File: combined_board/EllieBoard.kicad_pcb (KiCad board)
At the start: 2 copper layers, 54 parts, among them J1 Load Cell 1.1, J13 Load Cell 4.1, J14 Load Cell 5.1, J15 Load Cell 6.1, J2 Servo Conn 1, J22 Load Cell 7.1, J23 Load Cell 8.1, J28 Flow Meter Conn 2, J29 Servo Conn 2, J3 Servo Conn 3, J30 Servo Conn 4, J32 Load Cell 1.2, J33 Load Cell 2.2, J34 Load Cell 3.2, J35 Load Cell 4.2, J36 Load Cell 5.2, J37 Load Cell 6.2, J38 Load Cell 7.2, J39 Load Cell 8.2, J4 NC Conn, J41 Flow Meter Conn 1, J43 NC Conn, J5 NC Conn 2, J6 Load Cell 2.1, J7 NC Conn 2, J8 Load Cell 3.1, U1 HX711_Breakout, U10 HX711_Breakout, U11 HX711_Breakout, U2 HX711_Breakout, U3 Relay_Board, U4 SD_Card_Reader, U5 HX711_Breakout, U6 HX711_Breakout, U7 ESP32-DEVKITC-32D, U8 HX711_Breakout, U9 HX711_Breakout

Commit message: some updates to layout, not 100% done yet
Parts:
- moved R2 29.3 mm to (24.8, 144.8)
- moved U5 29.2 mm to (141.0, 99.1)
- moved J15 28.6 mm to (141.7, 154.4)
- moved J2 28.6 mm to (135.3, 34.3)
- moved J22 28.6 mm to (163.3, 154.3)
- moved J29 28.6 mm to (135.3, 19.1)
- moved J30 28.6 mm to (116.3, 19.1)
- moved J37 28.6 mm to (141.6, 165.1)
- moved J39 28.6 mm to (186.0, 165.1)
- moved J43 28.6 mm to (167.0, 33.0)
- moved J5 28.6 mm to (166.8, 21.1)
- moved R12 28.6 mm to (186.3, 146.1)
- moved R14 28.6 mm to (139.0, 146.0)
- moved R6 28.6 mm to (157.6, 145.9)
- moved U2 28.6 mm to (141.6, 127.0)
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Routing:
- net GND: track 0.00 -> 978.5 mm, vias 0 -> 2
- net +3V3: track 32.2 -> 386.7 mm, vias 0 -> 2
- net IO32: track 190.7 -> 472.6 mm, vias 0 -> 1
- net IO22: track 63.9 -> 244.9 mm, vias 0 -> 2
- net Lipo: track 0.00 -> 110.4 mm
- net SCK/CLK: track 78.7 -> 0.00 mm
- net SDO/SD0: track 75.7 -> 0.56 mm
- net IO14: track 74.1 -> 0.00 mm
- net IO23: track 72.0 -> 0.00 mm
- net IO27: track 71.5 -> 0.00 mm
- net IO26: track 68.6 -> 0.00 mm
- net IO2: track 61.1 -> 0.00 mm
- net IO34: track 60.8 -> 0.00 mm
- net IO16: track 60.1 -> 0.00 mm
- net SDI/SD1: track 53.0 -> 0.00 mm
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- removed copper zone on B.Cu, net +3V3
- removed copper zone on F.Cu, net GND
- removed copper zone on B.Cu, net Lipo
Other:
- board outline added: 222.9 x 165.1 mm

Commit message: Updated layout for review
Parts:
- moved J2 0.53 mm to (135.2, 34.8)
- moved R16 0.38 mm to (73.0, 145.1)
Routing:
- net IO32: track 472.6 -> 224.9 mm, vias 1 -> 2
- net IO22: track 244.9 -> 65.7 mm, vias 2 -> 1
- net GND: track 978.5 -> 806.7 mm
- net +3V3: track 386.7 -> 484.9 mm, vias 2 -> 3
- net SDO/SD0: track 0.56 -> 95.5 mm, vias 0 -> 1
- net IO2: track 0.00 -> 81.9 mm, vias 0 -> 2
- net IO23: track 0.00 -> 81.0 mm, vias 0 -> 1
- net SCK/CLK: track 0.00 -> 80.9 mm
- net IO14: track 0.00 -> 71.5 mm
- net IO27: track 0.00 -> 69.5 mm
- net IO26: track 0.00 -> 67.3 mm
- net IO16: track 0.00 -> 62.5 mm, vias 0 -> 1
- net IO34: track 0.00 -> 59.5 mm
- net SDI/SD1: track 0.00 -> 56.9 mm
- net IO35: track 56.7 -> 88.7 mm, vias 0 -> 1
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- added copper zone on B.Cu, net GND
- added copper zone on F.Cu, net GND
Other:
- board text added: "ELLIE"

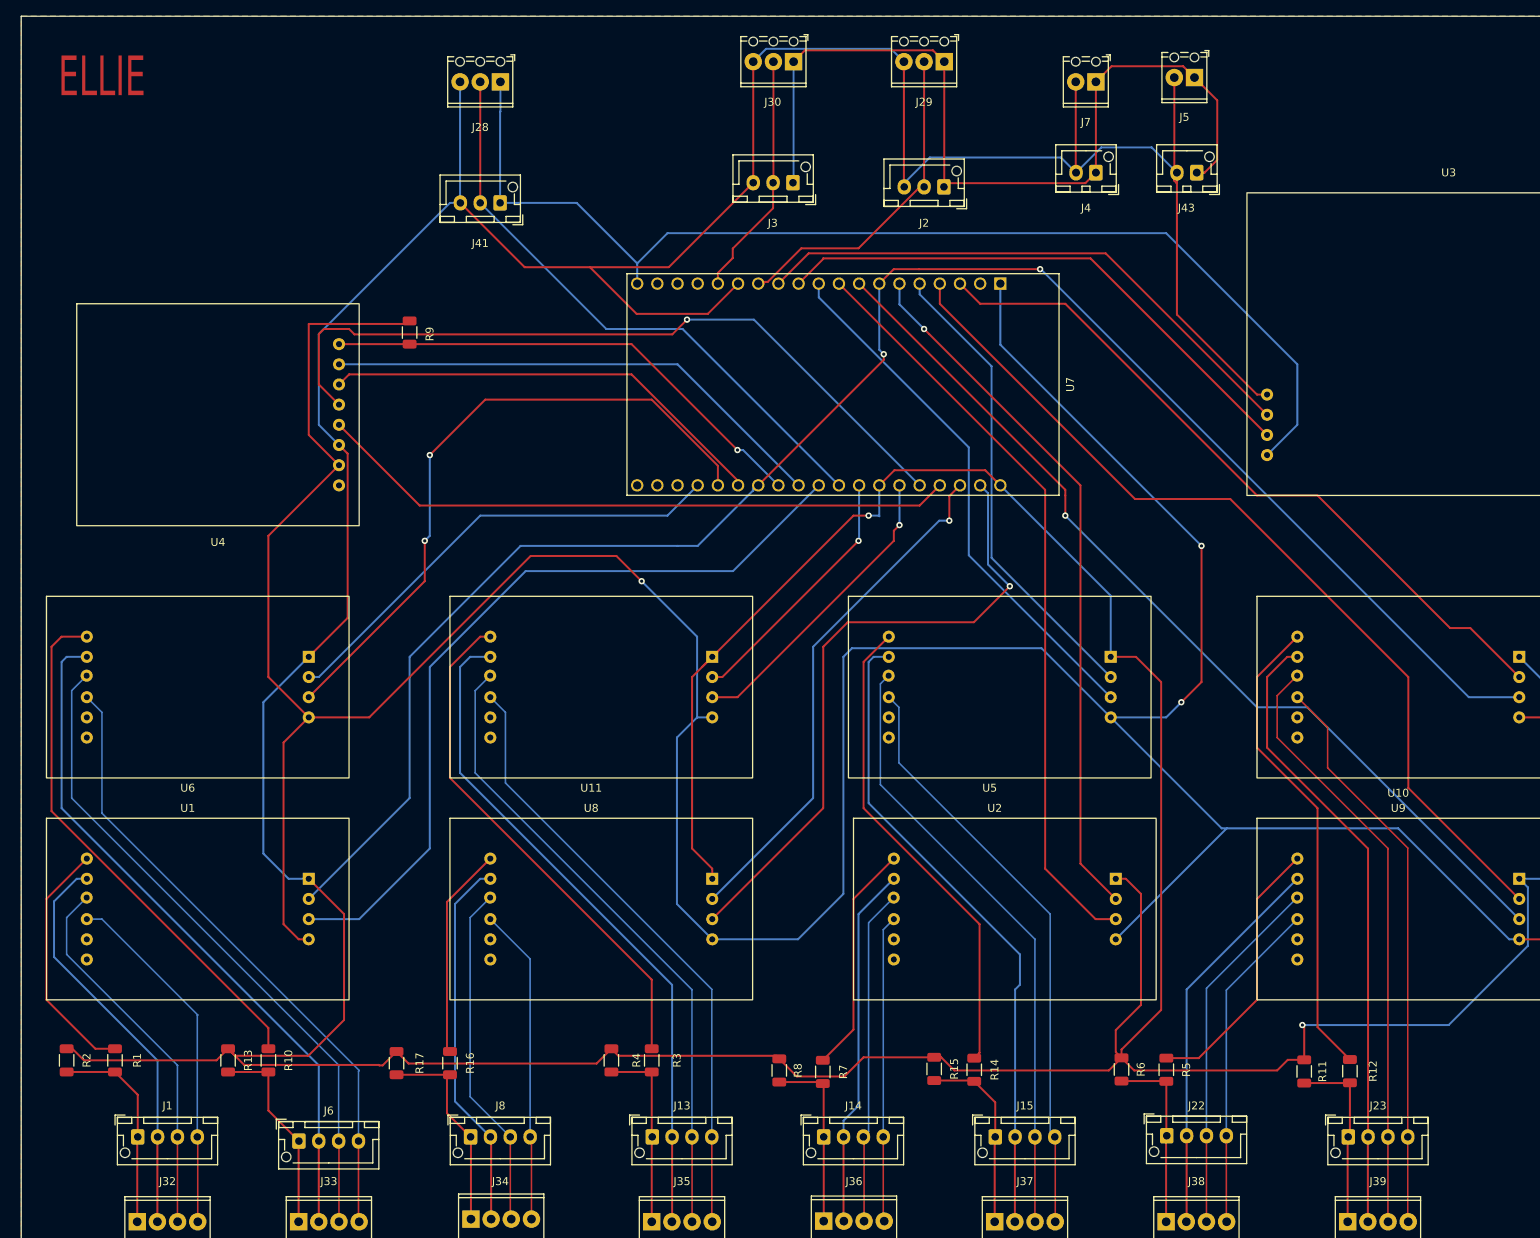
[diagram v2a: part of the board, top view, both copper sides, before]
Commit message: Updated layout for board, added silkscreen
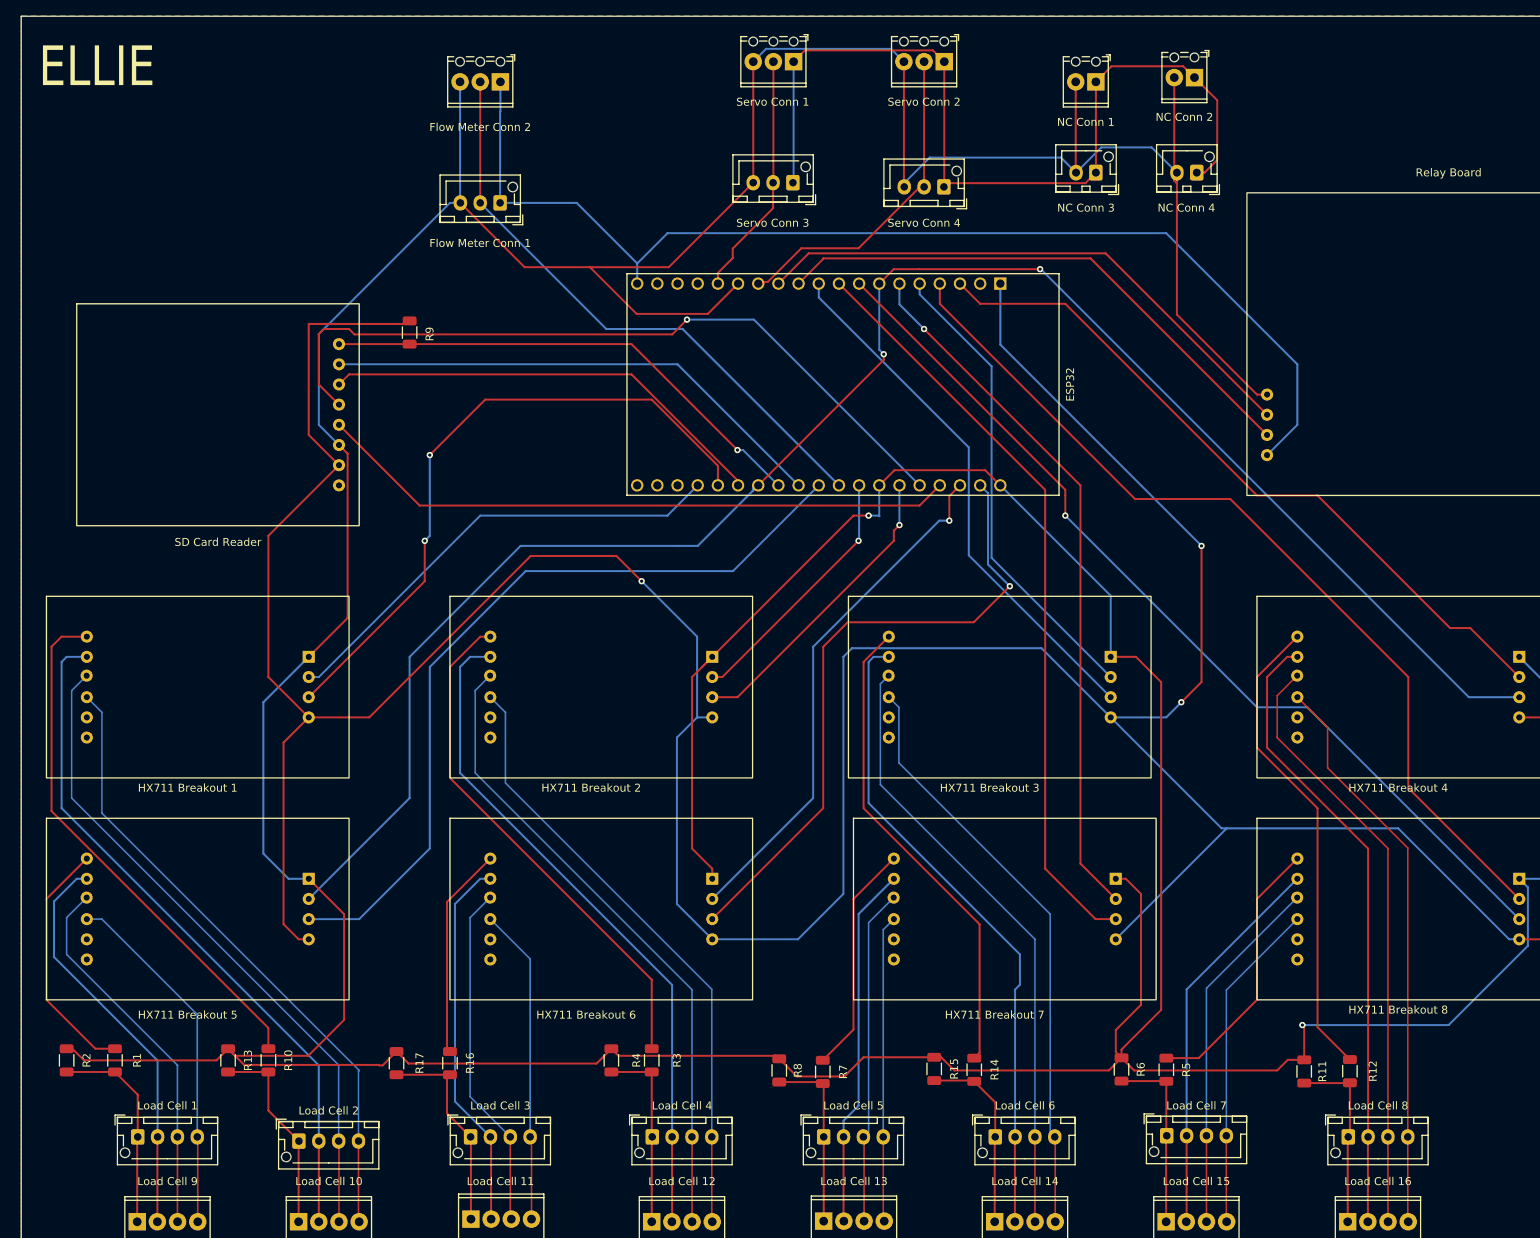
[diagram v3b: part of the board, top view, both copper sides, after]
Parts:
- Flow Meter Conn 1: renamed from J41
- Flow Meter Conn 2: renamed from J28
- HX711 Breakout 1: renamed from U6
- HX711 Breakout 2: renamed from U11
- HX711 Breakout 3: renamed from U5
- HX711 Breakout 4: renamed from U10
- HX711 Breakout 5: renamed from U1; value HX711_Breakout -> HX711 Breakout 5
- HX711 Breakout 6: renamed from U8; value HX711_Breakout -> HX711 Breakout 6
- HX711 Breakout 7: renamed from U2; value HX711_Breakout -> HX711 Breakout 7
- HX711 Breakout 8: renamed from U9; value HX711_Breakout -> HX711 Breakout 8
- Load Cell 1: renamed from J1
- Load Cell 10: renamed from J33
- Load Cell 11: renamed from J34
- Load Cell 12: renamed from J35
- Load Cell 13: renamed from J36
- Load Cell 14: renamed from J37
- Load Cell 15: renamed from J38
- Load Cell 16: renamed from J39
- Load Cell 2: renamed from J6
- Load Cell 3: renamed from J8
- Load Cell 4: renamed from J13
- Load Cell 5: renamed from J14
- Load Cell 6: renamed from J15
- Load Cell 7: renamed from J22
- Load Cell 8: renamed from J23
- Load Cell 9: renamed from J32
- NC Conn 1: renamed from J7
- NC Conn 2: renamed from J5
- NC Conn 3: renamed from J4
- NC Conn 4: renamed from J43
- Relay Board: renamed from U3
- SD Card Reader: renamed from U4
- Servo Conn 1: renamed from J30
- Servo Conn 2: renamed from J29
- Servo Conn 3: renamed from J3
- Servo Conn 4: renamed from J2
- renumbered U7 to ESP32

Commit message: Layout updates 04/05
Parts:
- added Battery: Battery Conn, Connector_JST:JST_XH_B2B-XH-AM_1x02_P2.50mm_Vertical, F.Cu at (184.8, 26.1)
- Flow Meter : renamed from Flow Meter Conn 1
- Flow Meter Backup: renamed from Flow Meter Conn 2
- Igniter 1: renamed from NC Conn 1; value NC Conn 2 -> Igniter 1
- Igniter 1 Backup: renamed from NC Conn 3
- Igniter 2: renamed from NC Conn 2
- Igniter 2 Backup: renamed from NC Conn 4
- Load Cell: renamed from Load Cell 4
- Load Cell : renamed from Load Cell 8
- Load Cell : renamed from Load Cell 2
- Load Cell : renamed from Load Cell 7
- Load Cell : renamed from Load Cell 3
- Load Cell : renamed from Load Cell 5
- Load Cell : renamed from Load Cell 6
- Load Cell : renamed from Load Cell 1
- Load Cell Backup: renamed from Load Cell 10
- Load Cell Backup: renamed from Load Cell 13
- Load Cell Backup: renamed from Load Cell 15
- Load Cell Backup: renamed from Load Cell 11
- Load Cell Backup: renamed from Load Cell 12
- Load Cell Backup: renamed from Load Cell 16
- Load Cell Backup: renamed from Load Cell 14
- Load Cell Backup: renamed from Load Cell 9
- Servo 1: renamed from Servo Conn 1
- Servo 1 Backup: renamed from Servo Conn 3
- Servo 2 : renamed from Servo Conn 2
- Servo 2 Backup: renamed from Servo Conn 4
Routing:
- net +3V3: track 484.9 -> 548.6 mm
- net GND: track 806.7 -> 828.9 mm, vias 2 -> 4
- net Lipo: track 110.4 -> 126.4 mm
- net IO14: track 71.5 -> 72.0 mm

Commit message: Layout changes 04/05
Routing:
- added copper zone on F.Cu, net Lipo
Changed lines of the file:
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@@
     (property "Sheetname" "")
     (attr through_hole)
-    (fp_text reference "Servo 1 Backup" (at 12.065 0.635 -90) (layer "F.SilkS")
+    (fp_text reference "Servo 1 Backup" (at 12.065 0.635 90) (layer "F.SilkS")
       (effects (font (size 1 1) (thickness 0.15)))
     )
@@
     (property "Sheetname" "")
     (attr through_hole)
-    (fp_text reference "Igniter 2 Backup" (at 1.31 -5.08) (layer "F.SilkS")
+    (fp_text reference "Igniter 2 Backup" (at -4.405 -0.635 -90) (layer "F.SilkS")
       (effects (font (size 1 1) (thickness 0.15)))
     )
@@
     (property "Sheetname" "")
     (attr through_hole)
-    (fp_text reference "Igniter 1 Backup" (at 2.58 -5.08) (layer "F.SilkS")
+    (fp_text reference "Igniter 1 Backup" (at 0.675 -5.08) (layer "F.SilkS")
       (effects (font (size 1 1) (thickness 0.15)))
     )
@@
   (zone (net 5) (net_name "GND") (layer "F.Cu") (hatch edge 0.508)
     (connect_pads (clearance 0.508))
-    (min_thickness 0.254)
-    (fill (thermal_gap 0.508) (thermal_bridge_width 0.508))
+    (min_thickness 0.254) (filled_areas_thickness no)
+    (fill yes (thermal_gap 0.508) (thermal_bridge_width 0.508))
+    (polygon
+      (pts
+        (xy 195.58 177.8)
+        (xy 97.79 178.435)
+        (xy 97.799841 40.639924)
+        (xy 165.351451 40.116436)
+        (xy 174.193929 43.797518)
+        (xy 173.952319 35.542518)
+        (xy 192.405 35.56)
+      )
+    )
+  )
+  (zone (net 5) (net_name "GND") (layer "F.Cu") (hatch edge 0.508)
+    (connect_pads (clearance 0.508))
+    (min_thickness 0.254) (filled_areas_thickness no)
+    (fill yes (thermal_gap 0.508) (thermal_bridge_width 0.508))
     (polygon
       (pts
         (xy 241.935 177.8)
-        (xy 19.05 178.435)
-        (xy 19.05 13.335)
+        (xy 197.810374 177.774045)
+        (xy 193.365374 13.309045)
         (xy 241.935 13.335)
       )
     )
   )
+  (zone (net 7) (net_name "Lipo") (layer "F.Cu") (hatch edge 0.508)
+    (connect_pads (clearance 0.508))
+    (min_thickness 0.254) (filled_areas_thickness no)
+    (fill yes (thermal_gap 0.508) (thermal_bridge_width 0.508))
+    (polygon
+      (pts
+        (xy 193.04 34.29)
+        (xy 172.72 34.29)
+        (xy 172.72 41.91)
+        (xy 166.37 39.37)
+        (xy 98.898737 39.276034)
+        (xy 99.06 14.605)
+        (xy 147.3708 14.605)
+        (xy 192.405 14.605)
+      )
+    )
+  )
+  (zone (net 5) (net_name "GND") (layer "F.Cu") (hatch edge 0.508)
+    (connect_pads (clearance 0.508))
+    (min_thickness 0.254) (filled_areas_thickness no)
+    (fill yes (thermal_gap 0.508) (thermal_bridge_width 0.508))
+    (polygon
+      (pts
+        (xy 97.79 178.435)
+        (xy 18.415 178.435)
+        (xy 18.415 13.335)
+        (xy 97.79 13.335)
+      )
+    )
+  )
   (zone (net 5) (net_name "GND") (layer "B.Cu") (hatch edge 0.508)
     (connect_pads (clearance 0.508))
-    (min_thickness 0.254)
-    (fill (thermal_gap 0.508) (thermal_bridge_width 0.508))
+    (min_thickness 0.254) (filled_areas_thickness no)
+    (fill yes (thermal_gap 0.508) (thermal_bridge_width 0.508))
     (polygon
       (pts
